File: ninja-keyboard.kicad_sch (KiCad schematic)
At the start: 259 parts, among them J1 Conn_01x05_Pin, J2 Conn_02x04_Counter_Clockwise, J3 USB_C_Receptacle_USB2.0_14P, J4 Conn_01x02, Q2 AO3401A, SW1 backquote, SW10 num9, SW11 num0, SW12 -, SW13 =, SW14 backsapce, SW15 tab, SW16 q, SW17 w, SW18 e, SW19 r, SW2 num1, SW20 t, SW21 y, SW22 u, SW23 i, SW24 o, SW25 p, SW26 [, SW27 ], SW28 \, SW29 cap, SW3 num2, SW30 a, SW31 s, SW32 d, SW33 f, SW34 h, SW35 g, SW36 j, SW37 k, SW38 l, SW39 semicolon, SW4 num3, SW40 apostrophe, SW41 enter, SW42 lshift, SW43 z, SW44 x, SW45 c, SW46 v, SW47 b, SW48 n, SW49 m, SW5 num4, SW50 comma, SW51 period, SW52 /, SW53 rshift, SW54 lctrl, SW55 win, SW56 lalt, SW57 space, SW58 ralt, SW59 win, SW6 num5, SW60 menu, SW61 rctrl, SW62 RotaryEncoder, SW63 SW_SPDT, SW7 num6, SW8 num7, SW9 num8, U1 ESP32-S3-WROOM-1, U2 TP4056-42-ESOP8

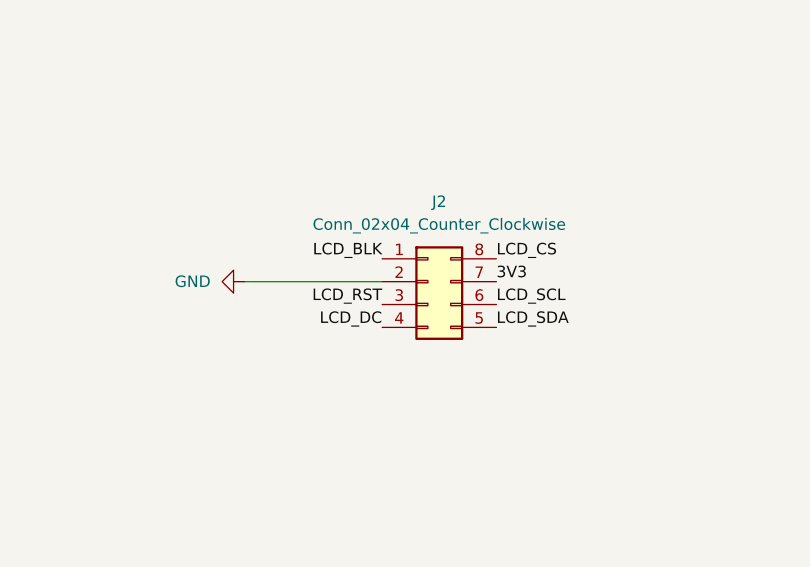
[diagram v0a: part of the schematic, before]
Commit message: Add a LCD sub board
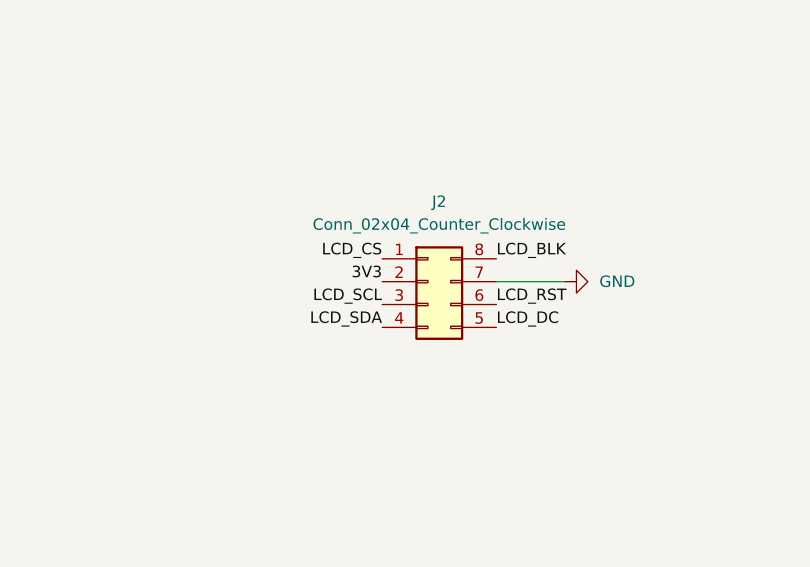
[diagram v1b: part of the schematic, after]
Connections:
- net 3V3: now also J2.2 (Pin_2); no longer J2.7 (Pin_7)
- net GND: now also J2.7 (Pin_7); no longer J2.2 (Pin_2)
- net LCD_BLK: now also J2.8 (Pin_8); no longer J2.1 (Pin_1)
- net LCD_CS: now also J2.1 (Pin_1); no longer J2.8 (Pin_8)
- net LCD_DC: now also J2.5 (Pin_5); no longer J2.4 (Pin_4)
- net LCD_RST: now also J2.6 (Pin_6); no longer J2.3 (Pin_3)
- net LCD_SCL: now also J2.3 (Pin_3); no longer J2.6 (Pin_6)
- net LCD_SDA: now also J2.4 (Pin_4); no longer J2.5 (Pin_5)
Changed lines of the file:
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@@
 	(wire
 		(pts
+			(xy 133.35 248.92) (xy 140.97 248.92)
+		)
+		(stroke
+			(width 0)
+			(type default)
+		)
+	)
+	(wire
+		(pts
 			(xy 114.3 68.58) (xy 149.86 68.58)
 		)
@@
 	(wire
 		(pts
-			(xy 105.41 248.92) (xy 120.65 248.92)
-		)
-		(stroke
-			(width 0)
-			(type default)
-		)
-	)
-	(wire
-		(pts
 			(xy 124.46 386.08) (xy 124.46 388.62)
 		)
@@
 	)
 	(label "LCD_CS"
-		(at 133.35 246.38 0)
+		(at 120.65 246.38 180)
 		(effects
 			(font
 				(size 1.27 1.27)
 			)
-			(justify left bottom)
+			(justify right bottom)
 		)
 	)
@@
 	)
 	(label "LCD_DC"
-		(at 120.65 254 180)
+		(at 133.35 254 0)
 		(effects
 			(font
 				(size 1.27 1.27)
 			)
-			(justify right bottom)
+			(justify left bottom)
 		)
 	)
@@
 	)
 	(label "LCD_BLK"
-		(at 120.65 246.38 180)
+		(at 133.35 246.38 0)
 		(effects
 			(font
 				(size 1.27 1.27)
 			)
-			(justify right bottom)
+			(justify left bottom)
 		)
 	)
@@
 	)
 	(label "LCD_SCL"
-		(at 133.35 251.46 0)
+		(at 120.65 251.46 180)
 		(effects
 			(font
 				(size 1.27 1.27)
 			)
-			(justify left bottom)
+			(justify right bottom)
 		)
 	)
@@
 	)
 	(label "LCD_SDA"
-		(at 133.35 254 0)
+		(at 120.65 254 180)
 		(effects
 			(font
 				(size 1.27 1.27)
 			)
-			(justify left bottom)
+			(justify right bottom)
 		)
 	)
@@
 	)
 	(label "3V3"
-		(at 133.35 248.92 0)
+		(at 120.65 248.92 180)
 		(effects
 			(font
 				(size 1.27 1.27)
 			)
-			(justify left bottom)
+			(justify right bottom)
 		)
 	)
@@
 	)
 	(label "LCD_RST"
-		(at 120.65 251.46 180)
+		(at 133.35 251.46 0)
 		(effects
 			(font
 				(size 1.27 1.27)
 			)
-			(justify right bottom)
+			(justify left bottom)
 		)
 	)
@@
 	(symbol
 		(lib_id "power:GND")
-		(at 105.41 248.92 270)
+		(at 140.97 248.92 90)
 		(unit 1)
 		(exclude_from_sim no)
@@
 		(fields_autoplaced yes)
 		(property "Reference" "#PWR0127"
-			(at 99.06 248.92 0)
+			(at 147.32 248.92 0)
 			(effects
 				(font
@@
 		)
 		(property "Value" "GND"
-			(at 101.6 248.9199 90)
+			(at 144.78 248.9199 90)
 			(effects
 				(font
@@
 		)
 		(property "Footprint" ""
-			(at 105.41 248.92 0)
+			(at 140.97 248.92 0)
 			(effects
 				(font
@@
 		)
 		(property "Datasheet" ""
-			(at 105.41 248.92 0)
+			(at 140.97 248.92 0)
 			(effects
 				(font
@@
 		)
 		(property "Description" "Power symbol creates a global label with name \"GND\" , ground"
-			(at 105.41 248.92 0)
+			(at 140.97 248.92 0)
 			(effects
 				(font

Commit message: 1. Use built in NTC resistors. 2. Correct the position of SL28.
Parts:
- removed J4: Conn_01x02, user_added:PH 1x2 pin gap 2.0mm SMD socket, symbol Connector_Generic:Conn_01x02
- removed R13: 10k B=3950 0805, Resistor_SMD:R_0805_2012Metric, symbol Device:R_Small
- added J5: Conn_01x03, Connector_JST:JST_PH_S3B-PH-K_1x03_P2.00mm_Horizontal, symbol Connector_Generic:Conn_01x03
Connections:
- net GND: now also J5.3 (Pin_3)
- net at SW63.2 (B): now also J5.1 (Pin_1)
- net NTC_PIN: now reaches C70.1, R10.2, R12.1, U2.1 (TEMP)
- net NTC_PIN: now also J5.2 (Pin_2)
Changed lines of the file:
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@@
 	)
 	(junction
-		(at 189.23 378.46)
+		(at 53.34 312.42)
 		(diameter 0)
 		(color 0 0 0 0)
 	)
 	(junction
-		(at 53.34 312.42)
+		(at 189.23 381)
 		(diameter 0)
 		(color 0 0 0 0)
@@
 	(wire
 		(pts
-			(xy 184.15 378.46) (xy 189.23 378.46)
+			(xy 184.15 381) (xy 189.23 381)
 		)
 		(stroke
@@
 	(wire
 		(pts
-			(xy 104.14 342.9) (xy 104.14 344.17)
-		)
-		(stroke
-			(width 0)
-			(type default)
-		)
-	)
-	(wire
-		(pts
 			(xy 182.88 116.84) (xy 175.26 116.84)
 		)
@@
 	(wire
 		(pts
-			(xy 104.14 335.28) (xy 104.14 337.82)
-		)
-		(stroke
-			(width 0)
-			(type default)
-		)
-	)
-	(wire
-		(pts
 			(xy 349.25 114.3) (xy 345.44 114.3)
 		)
@@
 	(wire
 		(pts
-			(xy 189.23 378.46) (xy 189.23 382.27)
+			(xy 189.23 381) (xy 189.23 384.81)
 		)
 		(stroke
@@
 	(wire
 		(pts
+			(xy 191.77 378.46) (xy 194.31 378.46)
+		)
+		(stroke
+			(width 0)
+			(type default)
+		)
+	)
+	(wire
+		(pts
 			(xy 181.61 171.45) (xy 182.88 171.45)
 		)
@@
 	(wire
 		(pts
-			(xy 104.14 344.17) (xy 92.71 344.17)
-		)
-		(stroke
-			(width 0)
-			(type default)
-		)
-	)
-	(wire
-		(pts
 			(xy 179.07 85.09) (xy 182.88 85.09)
 		)
@@
 	(wire
 		(pts
-			(xy 189.23 378.46) (xy 194.31 378.46)
+			(xy 189.23 381) (xy 194.31 381)
 		)
 		(stroke
@@
 	)
 	(label "BAT-"
-		(at 184.15 378.46 180)
+		(at 184.15 381 180)
 		(effects
 			(font
@@
 		)
 	)
+	(label "NTC_PIN"
+		(at 104.14 335.28 0)
+		(effects
+			(font
+				(size 1.27 1.27)
+			)
+			(justify left bottom)
+		)
+	)
 	(label "3V3"
 		(at 132.08 85.09 180)
@@
 		)
 	)
+	(label "NTC_PIN"
+		(at 191.77 378.46 180)
+		(effects
+			(font
+				(size 1.27 1.27)
+			)
+			(justify right bottom)
+		)
+	)
 	(label "3V3"
 		(at 386.08 144.78 180)
@@
 	(symbol
 		(lib_id "power:GND")
-		(at 189.23 382.27 0)
+		(at 189.23 384.81 0)
 		(unit 1)
 		(exclude_from_sim no)
@@
 		(dnp no)
 		(property "Reference" "#PWR0141"
-			(at 189.23 388.62 0)
+			(at 189.23 391.16 0)
 			(effects
 				(font
@@
 		)
 		(property "Value" "GND"
-			(at 189.357 386.6642 0)
+			(at 189.357 389.2042 0)
 			(effects
 				(font
@@
 		)
 		(property "Footprint" ""
-			(at 189.23 382.27 0)
+			(at 189.23 384.81 0)
 			(effects
 				(font
@@
 		)
 		(property "Datasheet" ""
-			(at 189.23 382.27 0)
+			(at 189.23 384.81 0)
 			(effects
 				(font
@@
 		)
 		(property "Description" "Power symbol creates a global label with name \"GND\" , ground"
-			(at 189.23 382.27 0)
+			(at 189.23 384.81 0)
 			(effects
 				(font
@@
 	)
 	(symbol
-		(lib_id "Connector_Generic:Conn_01x02")
-		(at 199.39 375.92 0)
-		(unit 1)
-		(exclude_from_sim no)
-		(in_bom yes)
-		(on_board yes)
-		(dnp no)
-		(property "Reference" "J4"
-			(at 197.3072 384.175 0)
-			(effects
-				(font
-					(size 1.27 1.27)
-				)
-			)
-		)
-		(property "Value" "Conn_01x02"
-			(at 197.3072 381.8636 0)
-			(effects
-				(font
-					(size 1.27 1.27)
-				)
-			)
-		)
-		(property "Footprint" "user_added:PH 1x2 pin gap 2.0mm SMD socket"
-			(at 199.39 375.92 0)
-			(effects
-				(font
-					(size 1.27 1.27)
-				)
-				(hide yes)
-			)
-		)
-		(property "Datasheet" "~"
-			(at 199.39 375.92 0)
-			(effects
-				(font
-					(size 1.27 1.27)
-				)
-				(hide yes)
-			)
-		)
-		(property "Description" "Generic connector, single row, 01x02, script generated (kicad-library-utils/schlib/autogen/connector/)"
-			(at 199.39 375.92 0)
-			(effects
-				(font
-					(size 1.27 1.27)
-				)
-				(hide yes)
-			)
-		)
-		(property "Sim.Device" ""
-			(at 199.39 375.92 0)
-			(effects
-				(font
-					(size 1.27 1.27)
-				)
-				(hide yes)
-			)
-		)
-		(property "Sim.Pins" ""
-			(at 199.39 375.92 0)
-			(effects
-				(font
-					(size 1.27 1.27)
-				)
-				(hide yes)
-			)
-		)
-		(property "LCSC Part #" "C7527581"
-			(at 199.39 375.92 0)
-			(effects
-				(font
-					(size 1.27 1.27)
-				)
-				(hide yes)
-			)
-		)
-		(pin "1"
-		)
-		(pin "2"
-		)
-		(instances
-			(project "ninja-keyboard"
-				(path "/38993bca-db6c-4f9a-9477-49e0546421f5"
-					(reference "J4")
-					(unit 1)
-				)
-			)
-		)
-	)
-	(symbol
 		(lib_id "Switch:SW_Push")
 		(at 391.16 171.45 0)
@@
 	)
 	(symbol
-		(lib_id "Device:R_Small")
-		(at 104.14 340.36 0)
-		(unit 1)
-		(exclude_from_sim no)
-		(in_bom yes)
-		(on_board yes)
-		(dnp no)
-		(fields_autoplaced yes)
-		(property "Reference" "R13"
-			(at 106.68 339.0899 0)
-			(effects
-				(font
-					(size 1.016 1.016)
-				)
-				(justify left)
-			)
-		)
-		(property "Value" "10k B=3950 0805"
-			(at 106.68 341.6299 0)
-			(effects
-				(font
-					(size 1.27 1.27)
-				)
-				(justify left)
-			)
-		)
-		(property "Footprint" "Resistor_SMD:R_0805_2012Metric"
-			(at 104.14 340.36 0)
-			(effects
-				(font
-					(size 1.27 1.27)
-				)
-				(hide yes)
-			)
-		)
-		(property "Datasheet" "~"
-			(at 104.14 340.36 0)
-			(effects
-				(font
-					(size 1.27 1.27)
-				)
-				(hide yes)
-			)
-		)
-		(property "Description" "Resistor, small symbol"
-			(at 104.14 340.36 0)
-			(effects
-				(font
-					(size 1.27 1.27)
-				)
-				(hide yes)
-			)
-		)
-		(property "LCSC Part #" "C95968"
-			(at 104.14 340.36 0)
-			(effects
-				(font
-					(size 1.27 1.27)
-				)
-			)
-		)
-		(pin "2"
-		)
-		(pin "1"
-		)
-		(instances
-			(project "ninja-keyboard"
-				(path "/38993bca-db6c-4f9a-9477-49e0546421f5"
-					(reference "R13")
-					(unit 1)
-				)
-			)
-		)
-	)
-	(symbol
 		(lib_id "Switch:SW_Push")
 		(at 162.56 110.49 0)
@@
 					(unit 1)
 				)
+			)
+		)
+	)
+	(symbol
+		(lib_id "Connector_Generic:Conn_01x03")
+		(at 199.39 378.46 0)
+		(unit 1)
+		(exclude_from_sim no)
+		(in_bom yes)
+		(on_board yes)
+		(dnp no)
+		(fields_autoplaced yes)
+		(property "Reference" "J5"
+			(at 201.93 377.1899 0)
+			(effects
+				(font
+					(size 1.27 1.27)
+				)
+				(justify left)
+			)
+		)
+		(property "Value" "Conn_01x03"
+			(at 201.93 379.7299 0)
+			(effects
+				(font
+					(size 1.27 1.27)
+				)
+				(justify left)
+			)
+		)
+		(property "Footprint" "Connector_JST:JST_PH_S3B-PH-K_1x03_P2.00mm_Horizontal"
+			(at 199.39 378.46 0)
+			(effects
+				(font
+					(size 1.27 1.27)
+				)
+				(hide yes)
+			)
+		)
+		(property "Datasheet" "~"
+			(at 199.39 378.46 0)
+			(effects
+				(font
+					(size 1.27 1.27)
+				)
+				(hide yes)
+			)
+		)
+		(property "Description" "Generic connector, single row, 01x03, script generated (kicad-library-utils/schlib/autogen/connector/)"
+			(at 199.39 378.46 0)
+			(effects
+				(font
+					(size 1.27 1.27)
+				)
+				(hide yes)
+			)
+		)
+		(pin "3"
+		)
+		(pin "1"
+		)
+		(pin "2"
+		)
+		(instances
+			(project ""
+				(path "/38993bca-db6c-4f9a-9477-49e0546421f5"
+					(reference "J5")
+					(unit 1)
+				)

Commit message: Add JLC sn to 1x3P 2mm connector
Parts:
- J5: LCSC Part # (none) -> C157929
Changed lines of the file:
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@@
+			)
+		)
+		(property "LCSC Part #" "C157929"
+			(at 199.39 378.46 0)
+			(effects
+				(font
+					(size 1.27 1.27)
+				)
+				(hide yes)
 			)
 		)
